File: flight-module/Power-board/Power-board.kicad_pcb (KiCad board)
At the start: 4 copper layers, 141.7 x 134.1 mm, 30 parts, among them J1 POWER, J10 PCIE, J2 PCIE, J3 XT60-M, J4 PCIE, J5 PCIE, J6 ESP32-DEVKITC-32D, J7 Conn_01x19_Male, J8 PCIE, J9 Conn_01x19_Male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

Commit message: power board
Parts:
- removed D1: D_Small, Diode_SMD:D_0603_1608Metric
- removed F4: 6A Fuse, Fuse:Fuse_2920_7451Metric
- removed G***: LOGO, star:star_8x7
- removed J10, J2, J4: PCIE, 10018784-10210TLF:AMPHENOL_10018784-10210TLF
- removed J3: XT60-M, XT60-M:AMASS_XT60-M
- removed J6: ESP32-DEVKITC-32D, Ellie_Project_Footprints:MODULE_ESP32-DEVKITC-32D
- removed J7, J9: Conn_01x19_Male, Connector_PinHeader_2.54mm:PinHeader_1x19_P2.54mm_Vertical
- removed R2: 1k, Resistor_SMD:R_0603_1608Metric
- removed REF**: DSUB-15_Female_Horizontal_P2.77x2.84mm_EdgePinOffset14.56mm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, Connector_Dsub:DSUB-15_Female_Horizontal_P2.77x2.84mm_EdgePinOffset14.56mm_Housed_MountingHolesOffset15.98mm
- removed REF**: Stack_Shape, Stack_Shape:Stack_Shape
- removed SW1: SW_SPST, Button_Switch_THT:SW_PUSH_6mm
- removed U2: 74HC4050D, 74HC4050D:SO16
- added C10: 22nF, Capacitor_SMD:C_0603_1608Metric, F.Cu at (137.5, 162.7)
- added C11: 0.1µF, Capacitor_SMD:C_0603_1608Metric, F.Cu at (137.5, 165.2)
- added C12: 10uF, Capacitor_SMD:C_0603_1608Metric, F.Cu at (137.5, 167.7)
- added C6: 22uF, Capacitor_SMD:C_0603_1608Metric, F.Cu at (133.5, 170.2)
- added C8: 22nF, Capacitor_SMD:C_0603_1608Metric, F.Cu at (137.5, 157.7)
- added C9: 22nF, Capacitor_SMD:C_0603_1608Metric, F.Cu at (137.5, 160.2)
- added D15: D_Schottky, Diode_SMD:D_0201_0603Metric, F.Cu at (154.0, 166.9)
- added D16: D_Schottky, Diode_SMD:D_0201_0603Metric, F.Cu at (154.0, 168.7)
- added D2: D_Small, Diode_SMD:D_0603_1608Metric, F.Cu at (154.5, 164.7)
- added R3: 10k, Resistor_SMD:R_0603_1608Metric, F.Cu at (141.5, 162.7)
- C4: value 22uF -> 22nF
- J1: value POWER -> Stack_Shape; footprint Connector:Banana_Jack_2Pin -> Stack_Shape:Stack_Shape
- J5: value PCIE -> POWER; footprint 10018784-10210TLF:AMPHENOL_10018784-10210TLF -> Connector:Banana_Jack_2Pin; moved to F.Cu
- J8: value PCIE -> XT60-M; footprint 10018784-10210TLF:AMPHENOL_10018784-10210TLF -> XT60-M:AMASS_XT60-M; moved to F.Cu
- R1: value 10k -> 1k
- U1, U4: footprint AZ1117IH-3:SOT230P700X185-4N -> AZ1117IH-3:SOT223_AZ1117I_6P5X3P5_DIO
- U3: value XTSD04GLGEAG -> TPS4H160BQPWPRQ1; footprint XTSD04GLGEAG:SON127P600X800X95-8N -> TPS4:PWP0028C_N
- moved J5 254.4 mm to (56.7, 162.5), turned to 0 degrees
- moved J1 217.8 mm to (123.2, 86.1), turned to 0 degrees
- moved U1 196.1 mm to (118.1, 161.3)
- moved U4 185.0 mm to (127.4, 161.3)
- moved C4 183.5 mm to (133.5, 165.2), turned to 0 degrees
- moved R1 179.3 mm to (141.5, 160.2), turned to 0 degrees
- moved C2 174.4 mm to (133.5, 160.2), turned to 0 degrees
- moved C5 173.3 mm to (133.5, 167.7), turned to 0 degrees
- moved F2 172.5 mm to (137.5, 170.2), turned to 0 degrees
- moved C1 170.6 mm to (133.5, 157.7)
- moved J8 170.6 mm to (102.8, 161.3), turned to 0 degrees
- moved C3 169.1 mm to (133.5, 162.7)
- moved F1 168.2 mm to (157.6, 159.9), turned to 0 degrees
- moved F3 164.2 mm to (141.5, 157.7), turned to 0 degrees
- moved U3 151.3 mm to (148.0, 162.1)
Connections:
- C1 pad 2: 3.3V -> +3.3V
- C2 pad 2: 12V -> V_ALL+
- C3 pad 2: 5V -> +5V
- C4 pad 1: GND -> LOX_VENT+
- C4 pad 2: Net-(C4-Pad2) -> GND
- C5 pad 2: 12V -> V_ALL+
- F1 pad 1: +12V -> /BAT1_+_pre
- F1 pad 2: Net-(C4-Pad2) -> /BAT1_+
- F2 pad 2: 3.3V -> +3.3V
- F3 pad 2: 5V -> +5V
- R1 pad 1: Net-(C4-Pad2) -> Net-(C12-Pad1)
- R1 pad 2: Net-(D1-Pad1) -> GND
- U1 pad 3: 12V -> V_ALL+
- U3 pad 1: unconnected-(U3-Pad1) -> GND
- U3 pad 2: SD CS_3.3 -> unconnected-(U3-NC-Pad2)
- U3 pad 3: SD CLK_3.3 -> PYRO1EN
- U3 pad 4: GND -> PYRO2EN
- U3 pad 5: SD MOSI_3.3 -> PYRO3EN
- U3 pad 6: SD, TC MISO -> PYRO4EN
- U3 pad 8: 3.3V -> unconnected-(U3-ST2_SEL_N-Pad8)
- U4 pad 3: 12V -> V_ALL+
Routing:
- net 12V: track 363.1 -> 0.00 mm, vias 3 -> 0
- net GND: track 350.6 -> 0.00 mm, vias 24 -> 0
- net 3.3V: track 293.4 -> 0.00 mm, vias 5 -> 0
- net HX CLK: track 262.4 -> 0.00 mm, vias 10 -> 0
- net HX3: track 262.4 -> 0.00 mm, vias 10 -> 0
- net SD, TC MISO: track 262.3 -> 0.00 mm, vias 9 -> 0
- net HX5: track 256.1 -> 0.00 mm, vias 7 -> 0
- net SD, TC CLK: track 241.9 -> 0.00 mm, vias 15 -> 0
- net HX7: track 241.6 -> 0.00 mm, vias 11 -> 0
- net TC2: track 240.4 -> 0.00 mm, vias 7 -> 0
- net HX1: track 237.9 -> 0.00 mm, vias 8 -> 0
- net HX6: track 236.2 -> 0.00 mm, vias 10 -> 0
- net HX8: track 233.8 -> 0.00 mm, vias 10 -> 0
- net TC CLK: track 223.3 -> 0.00 mm, vias 11 -> 0
- net TC MISO: track 215.4 -> 0.00 mm, vias 10 -> 0
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- added copper zone on In1.Cu, net GND
- removed copper zone on B.Cu, net GND
- removed copper zone on F.Cu, net GND
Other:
- board text removed: "+"
- board text removed: "-"
- board text removed: "3V3"
- board text removed: "A1"
- board text removed: "B1"
- board text removed: "Banana plug"
- board text removed: "Designed by: Khai Sam"
- board text removed: "EN"
- board text removed: "ESP32-DEVKITC-V4"
- board text removed: "GND"
- board text removed: "Ground DAQ 2 LE2 Hotfire 2023"
- board text removed: "HX CLK"
- board text removed: "HX1 DT"
- board text removed: "HX2 DT"
- board text removed: "HX3 DT"
- board text removed: "HX4 DT"
- board text removed: "HX5 DT"
- board text removed: "HX6 DT"
- board text removed: "HX7 DT"
- board text removed: "HX8 DT"
- board text removed: "I2C SCL"
- board text removed: "I2C SDA"
- board text removed: "PERIPHERAL 1"
- board text removed: "PERIPHERAL 2"
- board text removed: "PERIPHERAL 3"
- board text removed: "PERIPHERAL 4"
- board text removed: "PERIPHERAL 5"
- board text removed: "SD CLK"
- board text removed: "SD CS"
- board text removed: "SD MISO"
- board text removed: "SD MOSI"
- board text removed: "TC CLK"
- board text removed: "TC MISO"
- board text removed: "TC1 CS"
- board text removed: "TC2 CS"
- board text removed: "TC3 CS"
- board text removed: "TC4 CS"
- board text removed: "This side up"
- board text removed: "Wrong side"
- board text removed: "XT-60"

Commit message: did some power board layout
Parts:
- D15, D16: footprint Diode_SMD:D_0201_0603Metric -> Diode_SMD:D_0603_1608Metric
- moved J5 133.8 mm to (109.2, 39.4)
- moved J8 119.8 mm to (92.5, 41.9), turned to 180 degrees
- moved C2 116.6 mm to (66.5, 64.8), turned to 180 degrees
- moved F2 114.8 mm to (81.8, 69.8), turned to 180 degrees
- moved C6 113.9 mm to (138.4, 56.5), turned to 90 degrees
- moved U4 110.1 mm to (106.7, 53.2)
- moved C5 109.1 mm to (106.2, 62.1)
- moved U1 108.6 mm to (73.7, 62.2), turned to 90 degrees
- moved C1 103.5 mm to (76.7, 71.1), turned to 90 degrees
- moved D2 103.3 mm to (162.6, 61.7), turned to -90 degrees
- moved R3 103.1 mm to (157.9, 61.0)
- moved F1 102.6 mm to (145.2, 58.1)
- moved C4 98.4 mm to (124.9, 67.2), turned to 90 degrees
- moved C3 97.2 mm to (105.4, 69.7), turned to 90 degrees
- moved F3 96.7 mm to (107.4, 67.2), turned to 180 degrees
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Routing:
- added copper zone on In2.Cu, net V_ALL+

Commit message: some changes
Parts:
- D15, D16: footprint Diode_SMD:D_0603_1608Metric -> D_Schottky:SMADO-214AC_LEAD-FRAME_MCC
- moved C5 33.2 mm to (79.5, 81.9)
- moved U4 31.1 mm to (90.2, 79.5), turned to -90 degrees
- moved C3 29.6 mm to (77.2, 78.9)
- moved F3 26.7 mm to (83.1, 78.0)
- moved D2 24.4 mm to (138.4, 65.3), turned to 180 degrees
- moved D16 19.2 mm to (143.5, 95.6), turned to -90 degrees
- moved C12 17.4 mm to (148.6, 93.2), turned to 90 degrees
- moved U1 16.9 mm to (90.2, 66.0), turned to -90 degrees
- moved C10 16.8 mm to (117.3, 80.0), turned to 180 degrees
- moved R3 16.5 mm to (142.2, 66.0), turned to 180 degrees
- moved D15 16.2 mm to (153.7, 95.6)
- moved C9 14.7 mm to (121.9, 79.2), turned to -90 degrees
- moved C2 13.8 mm to (79.8, 68.3), turned to 0 degrees
- moved R1 13.2 mm to (149.0, 97.8)
- moved J8 8.17 mm to (95.5, 49.5)
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
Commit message: routing not done
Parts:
- J8: footprint XT60-M:AMASS_XT60-M -> Connector_AMASS:AMASS_XT60PW-F_1x02_P7.20mm_Horizontal
- moved F1 59.5 mm to (157.4, 116.3)
- moved J8 59.3 mm to (154.4, 55.8), turned to 90 degrees
- moved C6 49.4 mm to (148.6, 109.8)
- moved R3 48.5 mm to (147.8, 114.2)
- moved D2 48.4 mm to (143.0, 113.4), turned to 90 degrees
- moved J5 31.3 mm to (140.5, 41.4), turned to 180 degrees
- moved C8 23.1 mm to (131.7, 82.5), turned to 0 degrees
- moved C10 17.2 mm to (131.7, 89.4), turned to 0 degrees
- moved C11 14.9 mm to (121.7, 94.2)
- moved U3 13.4 mm to (121.9, 84.8)
- moved C4 13.0 mm to (131.7, 79.6)
- moved C9 12.3 mm to (131.7, 86.8), turned to 0 degrees
- moved C5 11.4 mm to (89.2, 87.8)
- moved C2 9.55 mm to (89.0, 65.8)
- moved U1 5.17 mm to (89.2, 71.1)
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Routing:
- net PYRO4EN: track 0.00 -> 97.2 mm
- net PYRO3EN: track 0.00 -> 91.6 mm
- net PWR_SUP: track 0.00 -> 91.1 mm
- net PYRO2EN: track 0.00 -> 86.7 mm
- net ETH_VENT+: track 0.00 -> 73.3 mm, vias 0 -> 2
- net LOX_VENT+: track 0.00 -> 64.5 mm, vias 0 -> 2
- net PYRO_EX+: track 0.00 -> 62.0 mm
- net PYRO1EN: track 0.00 -> 59.8 mm
- net /BAT1_+: track 0.00 -> 25.5 mm
- net +5V: track 0.00 -> 15.1 mm
- net +3.3V: track 0.00 -> 10.6 mm
- net GND: track 0.00 -> 9.82 mm, vias 0 -> 1
- net ETH_MAIIN+: track 0.00 -> 6.81 mm
- net /BAT1_+_pre: track 0.00 -> 5.47 mm, vias 0 -> 1
- net Net-(U4-OUTPUT): track 0.00 -> 3.70 mm
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
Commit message: power board done?
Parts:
- moved D16 67.6 mm to (80.0, 100.8)
- moved F1 32.5 mm to (156.6, 83.8)
- moved D2 28.3 mm to (143.5, 85.2)
- moved R3 28.2 mm to (147.7, 86.0)
- moved C6 27.1 mm to (148.7, 82.7)
- moved C11 16.9 mm to (138.4, 92.0)
- moved C2 10.4 mm to (89.1, 76.2), turned to 180 degrees
- moved J8 3.93 mm to (153.2, 52.1)
- moved J5 3.79 mm to (139.3, 37.8)
- moved D15 0.72 mm to (157.2, 95.7)
- moved J1 0.06 mm to (123.2, 86.1)
- turned C5 to 180 degrees
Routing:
- net /BAT1_+_pre: track 5.47 -> 80.9 mm, vias 1 -> 2
- net PWR_SUP: track 91.1 -> 21.8 mm
- net GND: track 9.82 -> 61.7 mm, vias 1 -> 20
- net /BAT1_+: track 25.5 -> 10.1 mm
- net Net-(D2-K): track 0.00 -> 3.40 mm
- net +5V: track 15.1 -> 18.4 mm
- net V_ALL+: track 0.00 -> 3.19 mm, vias 0 -> 33
- net Net-(C12-Pad1): track 0.00 -> 2.98 mm
- net ETH_MAIN+: track 0.00 -> 2.00 mm
- added copper zone on F.Cu, net V_ALL+

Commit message: power v2
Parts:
- removed J8: XT60-M, Connector_AMASS:AMASS_XT60PW-F_1x02_P7.20mm_Horizontal
- added G***: LOGO, star:star_8x7, F.Cu at (122.4, 107.4)
- added J2: XT60-M, Connector_AMASS:AMASS_XT60PW-F_1x02_P7.20mm_Horizontal, F.Cu at (153.2, 52.1)
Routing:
- net /BAT1_+_pre: track 80.9 -> 73.8 mm
- net GND: track 61.7 -> 61.0 mm
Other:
- board text added: "Flight Module Power Board V2"

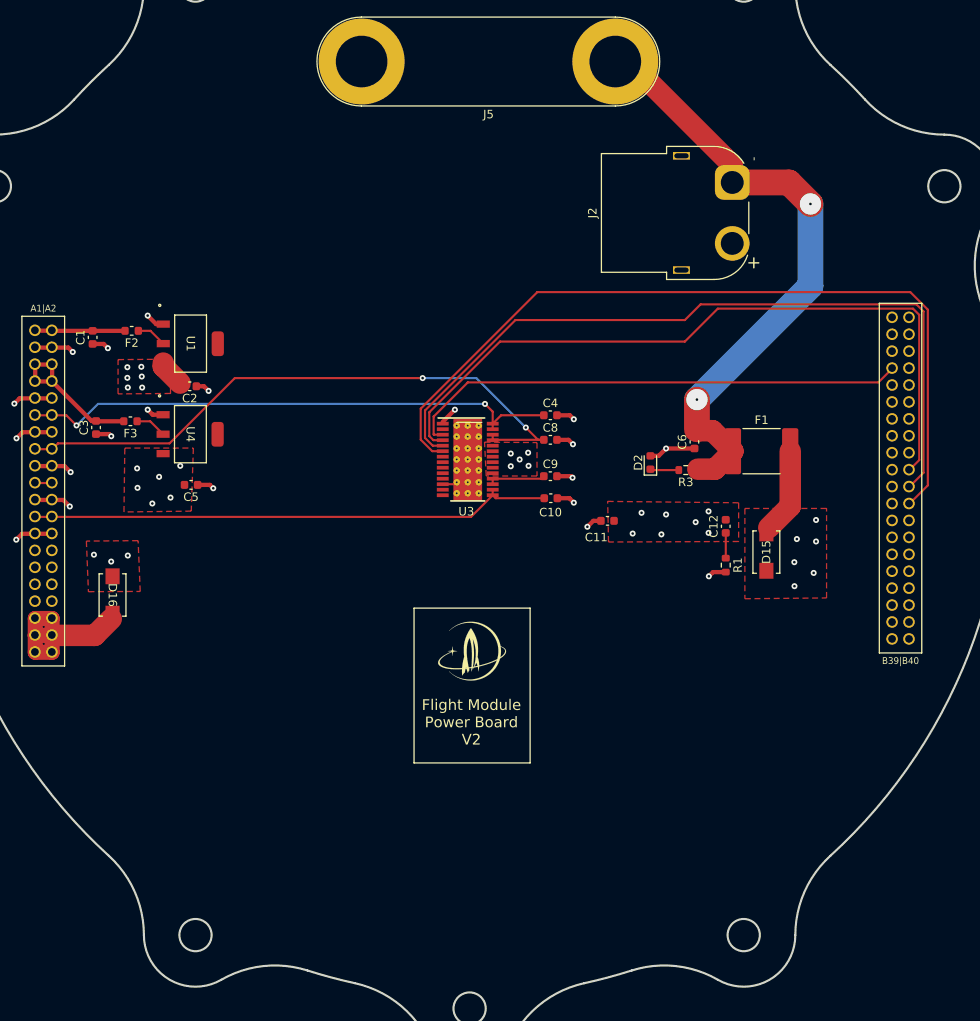
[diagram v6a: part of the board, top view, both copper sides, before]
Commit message: leds + redundancy, still getting footprint errors
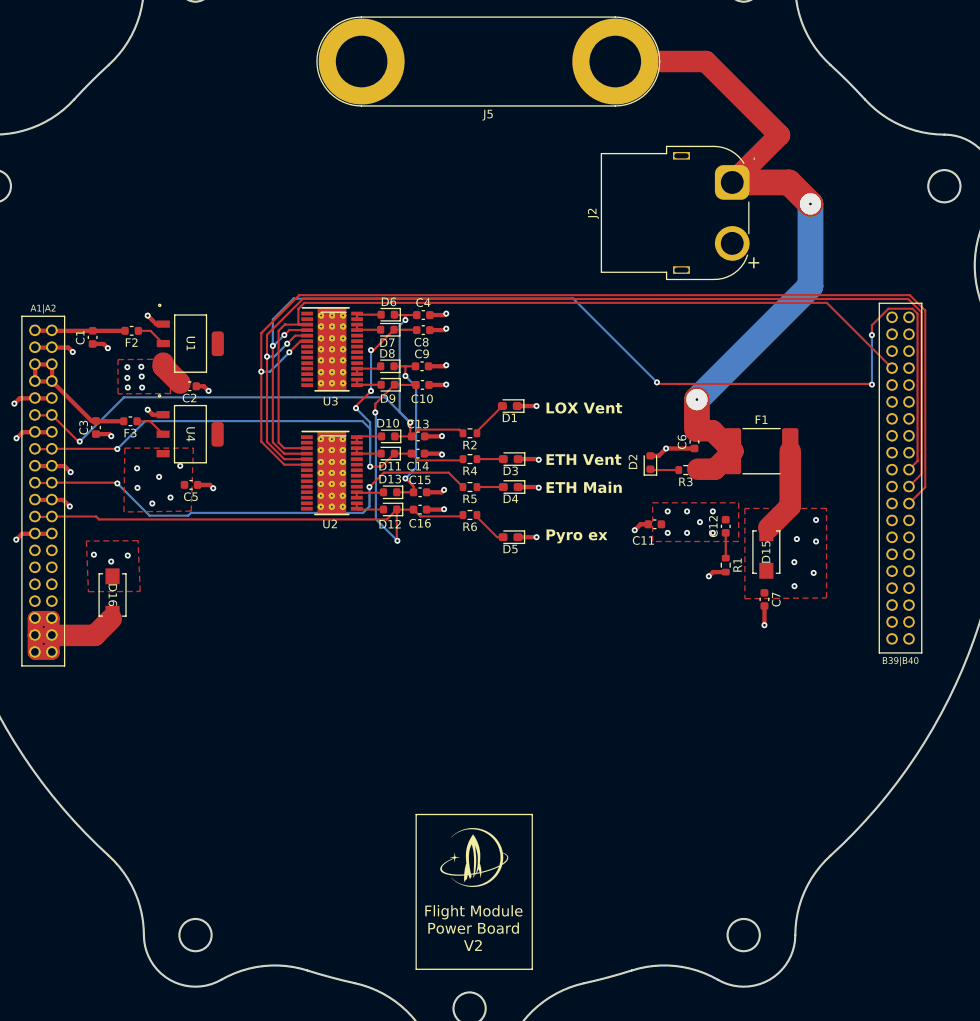
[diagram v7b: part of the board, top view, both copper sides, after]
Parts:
- added C13: 22nF, Capacitor_SMD:C_0603_1608Metric, F.Cu at (116.1, 82.1)
- added C14: 22nF, Capacitor_SMD:C_0603_1608Metric, F.Cu at (116.0, 84.1)
- added C15: 22nF, Capacitor_SMD:C_0603_1608Metric, F.Cu at (116.3, 88.7)
- added C16: 22nF, Capacitor_SMD:C_0603_1608Metric, F.Cu at (116.3, 90.7)
- added C7: 0.1µF, Capacitor_SMD:C_0603_1608Metric, F.Cu at (157.0, 101.3)
- added D1: LED, LED_SMD:LED_0603_1608Metric_Pad1.05x0.95mm_HandSolder, F.Cu at (126.9, 78.5)
- added D10: D_Small, Diode_SMD:D_0603_1608Metric, F.Cu at (112.5, 82.1)
- added D11: D_Small, Diode_SMD:D_0603_1608Metric, F.Cu at (112.5, 84.1)
- added D12: D_Small, Diode_SMD:D_0603_1608Metric, F.Cu at (112.7, 90.7)
- added D13: D_Small, Diode_SMD:D_0603_1608Metric, F.Cu at (112.7, 88.7)
- added D3: LED, LED_SMD:LED_0603_1608Metric_Pad1.05x0.95mm_HandSolder, F.Cu at (127.0, 84.8)
- added D4: LED, LED_SMD:LED_0603_1608Metric_Pad1.05x0.95mm_HandSolder, F.Cu at (127.0, 88.1)
- added D5: LED, LED_SMD:LED_0603_1608Metric_Pad1.05x0.95mm_HandSolder, F.Cu at (127.0, 94.0)
- added D6: D_Small, Diode_SMD:D_0603_1608Metric, F.Cu at (112.5, 67.7)
- added D7: D_Small, Diode_SMD:D_0603_1608Metric, F.Cu at (112.4, 69.5)
- added D8: D_Small, Diode_SMD:D_0603_1608Metric, F.Cu at (112.4, 73.8)
- added D9: D_Small, Diode_SMD:D_0603_1608Metric, F.Cu at (112.5, 76.0)
- added R2: 2k, Resistor_SMD:R_0603_1608Metric, F.Cu at (122.2, 81.7)
- added R4: 2k, Resistor_SMD:R_0603_1608Metric, F.Cu at (122.2, 84.8)
- added R5: 2k, Resistor_SMD:R_0603_1608Metric, F.Cu at (122.2, 88.1)
- added R6: 2k, Resistor_SMD:R_0603_1608Metric, F.Cu at (122.2, 91.4)
- added U2: TPS4H160BQPWPRQ1, TPS4:PWP0028C_N, F.Cu at (105.9, 86.4)
- moved G*** 24.4 mm to (122.7, 131.8)
- moved U3 20.6 mm to (105.9, 71.8)
- moved C10 20.2 mm to (116.6, 76.0)
- moved C9 20.0 mm to (116.5, 73.8)
- moved C8 19.8 mm to (116.7, 69.5)
- moved C4 19.1 mm to (116.7, 67.7)
- moved C11 5.61 mm to (144.0, 92.5)
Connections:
- U3 pad 15: PYRO_EX+ -> Net-(D9-A)
- U3 pad 16: PYRO_EX+ -> Net-(D9-A)
- U3 pad 17: ETH_MAIIN+ -> Net-(D8-A)
- U3 pad 18: ETH_MAIIN+ -> Net-(D8-A)
- U3 pad 25: ETH_VENT+ -> Net-(D7-A)
- U3 pad 26: ETH_VENT+ -> Net-(D7-A)
- U3 pad 27: LOX_VENT+ -> Net-(D6-A)
- U3 pad 28: LOX_VENT+ -> Net-(D6-A)
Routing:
- net ETH_MAIN+: track 2.00 -> 56.3 mm, vias 0 -> 2
- net PYRO2EN: track 86.7 -> 132.2 mm, vias 0 -> 5
- net PYRO1EN: track 59.8 -> 97.0 mm
- net PYRO4EN: track 97.2 -> 130.9 mm, vias 0 -> 2
- net PYRO3EN: track 91.6 -> 124.9 mm, vias 0 -> 2
- net PYRO_EX+: track 62.0 -> 78.3 mm, vias 0 -> 2
- net GND: track 61.0 -> 77.4 mm, vias 20 -> 28
- net ETH_MAIIN+: track 6.81 -> 20.8 mm, vias 0 -> 2
- net LOX_VENT+: track 64.5 -> 75.5 mm, vias 2 -> 3
- net /BAT1_+_pre: track 73.8 -> 83.7 mm
- net ETH_VENT+: track 73.3 -> 78.4 mm, vias 2 -> 5
- net Net-(D1-A): track 0.00 -> 4.46 mm
- net Net-(D5-A): track 0.00 -> 4.32 mm
- net Net-(D13-A): track 0.00 -> 3.86 mm
- net Net-(D12-A): track 0.00 -> 3.84 mm
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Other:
- board text added: "ETH Main"
- board text added: "ETH Vent"
- board text added: "LOX Vent"
- board text added: "Pyro ex"
